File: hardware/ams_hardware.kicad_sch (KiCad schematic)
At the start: 73 parts, among them J1 USB2UART, J2 1.47 IPS LCD, J3 ConnBattery, J4 RTD_PT100, Q1 SS8050, Q2 SS8050, Q3 SS8050, SW1 RST, SW2 IN1, SW3 Boot, SW4 IN2, SW5 IN4, SW6 IN4, SW7 IN5, U1 CH340C, U2 ESP32-S3-WROOM-1, U3 TPS63001_SEPIC_3V3, U4 MAX31865xTP, U5 BQ24075RGT_DPPM

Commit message: feat: add pi zero 2 w in schematic
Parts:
- added A1: Raspberry Pi Zero v1.3, Raspberry_Pi_Zero_v.1.3_Hat:RASPI_ZERO_FULL, symbol Raspberry_Pi_Zero_v.1.3_Hat:Raspberry_Pi_Zero_v.1.3_Hat

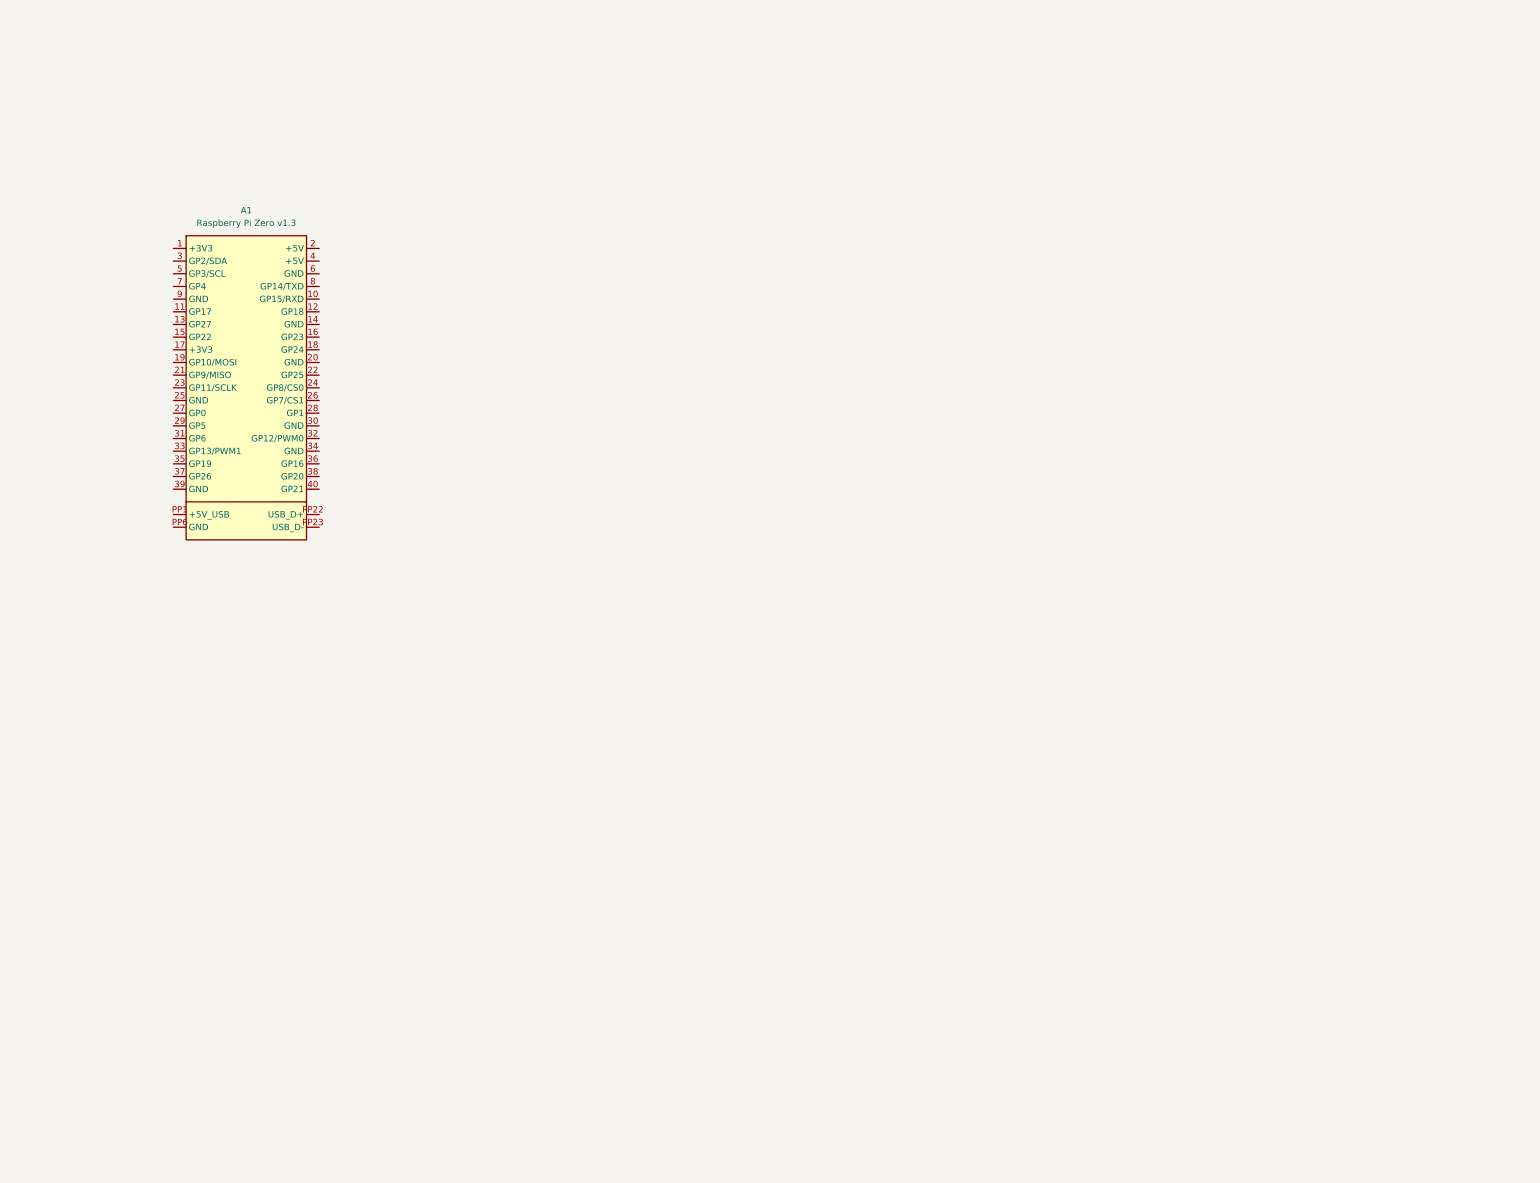
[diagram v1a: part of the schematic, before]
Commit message: feat: add logic to turn on and turn of pi
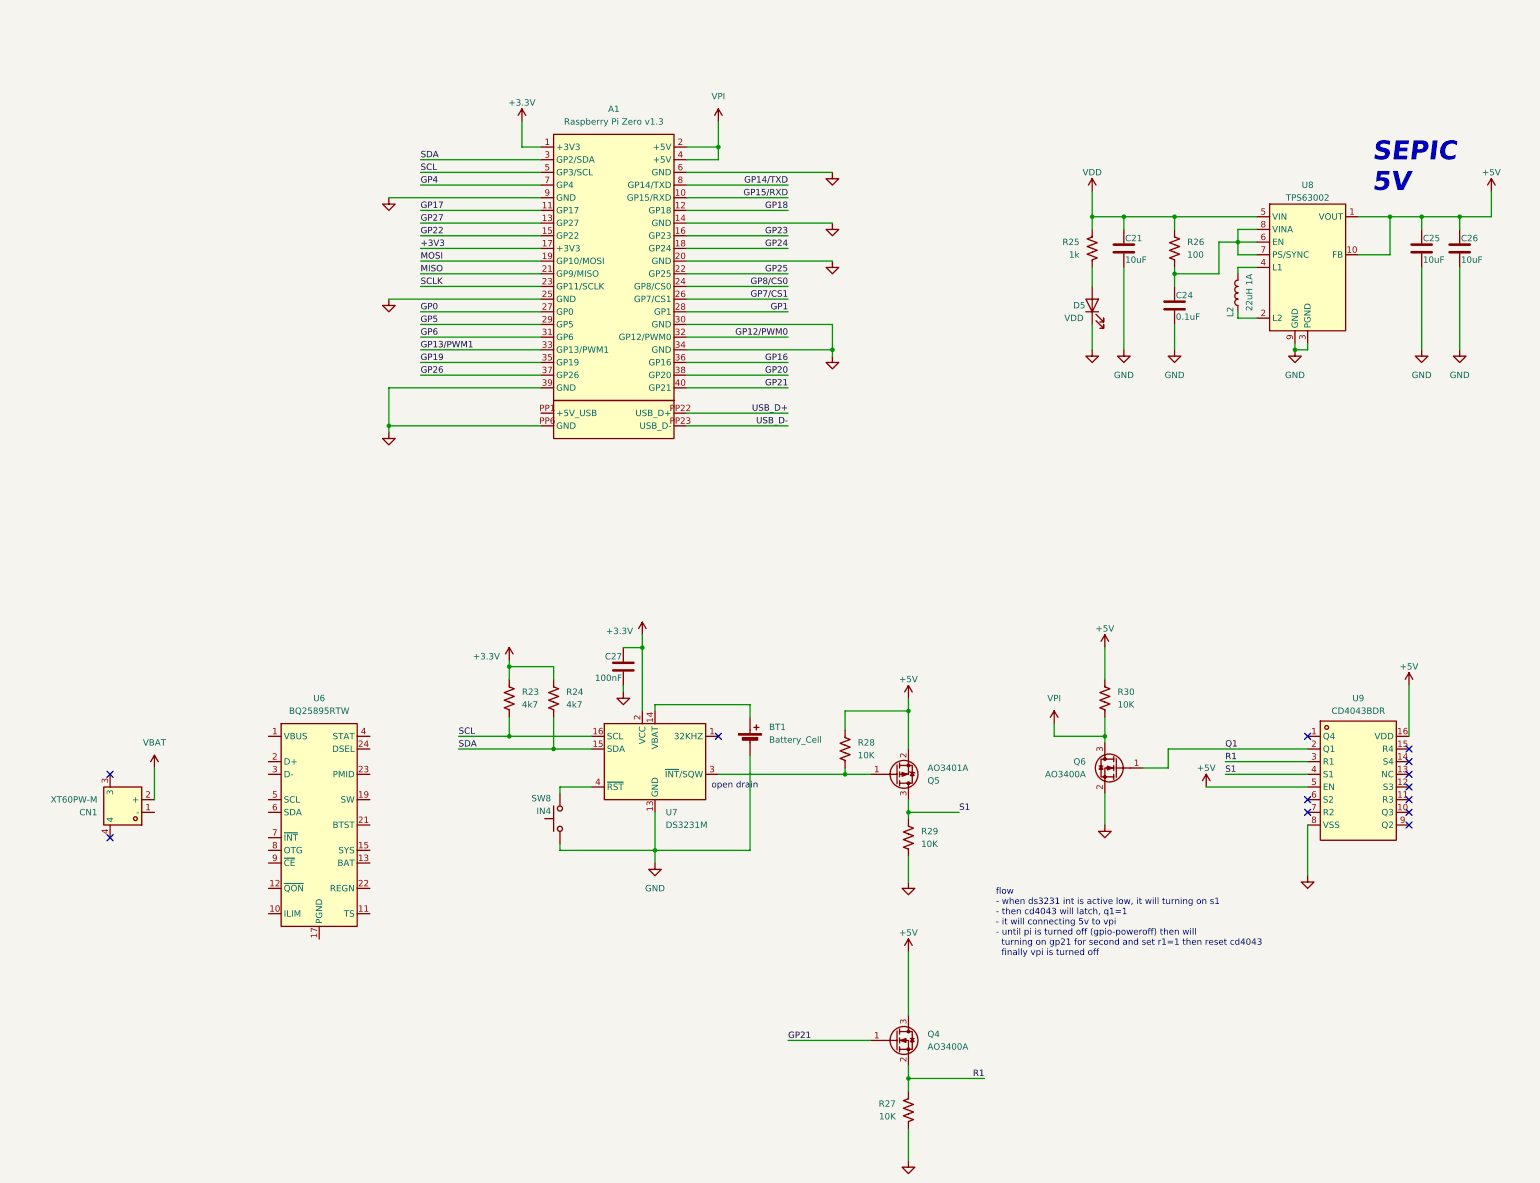
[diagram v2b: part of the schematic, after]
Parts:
- added BT1: Battery_Cell, Battery:BatteryHolder_Keystone_3002_1x2032, symbol Device:Battery_Cell
- added C21, C25, C26: 10uF, Capacitor_SMD:C_0805_2012Metric_Pad1.18x1.45mm_HandSolder, symbol Device:C
- added C24: 0.1uF, Capacitor_SMD:C_0805_2012Metric_Pad1.18x1.45mm_HandSolder, symbol Device:C
- added C27: 100nF, Capacitor_SMD:C_0805_2012Metric_Pad1.18x1.45mm_HandSolder, symbol Device:C
- added CN1: XT60PW-M, easyeda2kicad:CONN-TH_XT60PW-M, symbol easyeda2kicad:XT60PW-M
- added D5: VDD, LED_SMD:LED_1206_3216Metric_Pad1.42x1.75mm_HandSolder, symbol Device:LED
- added L2: 22uH 1A, Inductor_SMD:L_Bourns_SRP7028A_7.3x6.6mm, symbol Device:L
- added Q4, Q6: AO3400A, Package_TO_SOT_SMD:SOT-23W_Handsoldering, symbol Transistor_FET:AO3400A
- added Q5: AO3401A, Package_TO_SOT_SMD:SOT-23W_Handsoldering, symbol Transistor_FET:AO3401A
- added R23, R24: 4k7, Resistor_SMD:R_0805_2012Metric_Pad1.20x1.40mm_HandSolder, symbol Device:R_US
- added R25: 1k, Resistor_SMD:R_0805_2012Metric_Pad1.20x1.40mm_HandSolder, symbol Device:R_US
- added R26: 100, Resistor_SMD:R_0805_2012Metric_Pad1.20x1.40mm_HandSolder, symbol Device:R_US
- added R27, R28, R29, R30: 10K, Resistor_SMD:R_0805_2012Metric_Pad1.20x1.40mm_HandSolder, symbol Device:R_US
- added SW8: IN4, Button_Switch_SMD:SW_SPST_Omron_B3FS-100xP, symbol Switch:SW_Push
- added U6: BQ25895RTW, Package_DFN_QFN:Texas_RTW_WQFN-24-1EP_4x4mm_P0.5mm_EP2.7x2.7mm_ThermalVias, symbol Battery_Management:BQ25895RTW
- added U7: DS3231M, Package_SO:SOIC-16W_7.5x10.3mm_P1.27mm, symbol Timer_RTC:DS3231M
- added U8: TPS63002, Package_SON:Texas_DRC0010J_ThermalVias, symbol Regulator_Switching:TPS63002
- added U9: CD4043BDR, easyeda2kicad:SOIC-16_L9.9-W3.9-P1.27-LS6.0-BL, symbol easyeda2kicad:CD4043BDR
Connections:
- net +3.3V: now also A1.1 (+3V3), C27.1, R23.1, R24.1, U7.2 (VCC)
- net GND: now also A1.14 (GND), A1.20 (GND), A1.25 (GND), A1.30 (GND), A1.34 (GND), A1.39 (GND), A1.6 (GND), A1.9 (GND), A1.PP6 (GND), BT1.2 (-), C21.2, C24.2, C25.2, C26.2, C27.2, D5.1 (K), Q6.2 (S), R27.2, R29.2, SW8.1, U7.10 (GND), U7.11 (GND), U7.12 (GND), U7.13 (GND), U7.5 (GND), U7.6 (GND), U7.7 (GND), U7.8 (GND), U7.9 (GND), U8.11 (PGND), U8.3 (PGND), U8.9 (GND), U9.8 (VSS)
- net MISO: now also A1.21 (GP9/MISO)
- net MOSI: now also A1.19 (GP10/MOSI)
- net VDD: now also C21.1, R25.1, R26.1, U8.5 (VIN)
- net GP15/RXD: now reaches A1.10 (GP15/RXD)
- net GP17: now reaches A1.11 (GP17)
- net GP18: now reaches A1.12 (GP18)
- net GP27: now reaches A1.13 (GP27)
- net GP22: now reaches A1.15 (GP22)
- net GP23: now reaches A1.16 (GP23)
- net +3V3: now reaches A1.17 (+3V3)
- net GP24: now reaches A1.18 (GP24)
- net VPI: now reaches A1.2 (+5V)
- net VPI: now also A1.4 (+5V), Q6.3 (D), R30.2
- net GP25: now reaches A1.22 (GP25)
- net SCLK: now reaches A1.23 (GP11/SCLK)
- net GP8/CS0: now reaches A1.24 (GP8/CS0)
- net GP7/CS1: now reaches A1.26 (GP7/CS1)
- net GP0: now reaches A1.27 (GP0)
- net GP1: now reaches A1.28 (GP1)
- net GP5: now reaches A1.29 (GP5)
- net SDA: now reaches A1.3 (GP2/SDA)
- net SDA: now also R24.2, U7.15 (SDA)
- net GP6: now reaches A1.31 (GP6)
- net GP12/PWM0: now reaches A1.32 (GP12/PWM0)
- net GP13/PWM1: now reaches A1.33 (GP13/PWM1)
- net GP19: now reaches A1.35 (GP19)
- net GP16: now reaches A1.36 (GP16)
- net GP26: now reaches A1.37 (GP26)
- net GP20: now reaches A1.38 (GP20)
- net GP21: now reaches A1.40 (GP21)
- net GP21: now also Q4.1 (G)
- net SCL: now reaches A1.5 (GP3/SCL)
- net SCL: now also R23.2, U7.16 (SCL)
- net GP4: now reaches A1.7 (GP4)
- net GP14/TXD: now reaches A1.8 (GP14/TXD)
- net USB_D+: now reaches A1.PP22 (USB_D+)
- net USB_D-: now reaches A1.PP23 (USB_D-)
- new net: Q5.1 (G), R28.2, U7.3 (~{INT}/SQW)
- new net: D5.2 (A), R25.2
- new net: BT1.1 (+), U7.14 (VBAT)
- new net: SW8.2, U7.4 (~{RST})
- new net: C24.1, R26.2, U8.6 (EN), U8.7 (PS/SYNC), U8.8 (VINA)
- new net: U6.13 (BAT), U6.14 (BAT)
- new net: U6.15 (SYS), U6.16 (SYS)
- new net: U6.17 (PGND), U6.18 (PGND), U6.25 (PGND)
- new net: U6.19 (SW), U6.20 (SW)
- new net: L2.1, U8.2 (L2)
- new net: L2.2, U8.4 (L1)
- new net +5V: C25.1, C26.1, Q4.3 (D), Q5.2 (S), R28.1, R30.1, U8.1 (VOUT), U8.10 (FB), U9.16 (VDD), U9.5 (EN)
- new net Q1: Q6.1 (G), U9.2 (Q1)
- new net R1: Q4.2 (S), R27.1, U9.3 (R1)
- new net S1: Q5.3 (D), R29.1, U9.4 (S1)
- new net VBAT: CN1.2 (+)
- no-connect marks 24 -> 37
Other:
- note added: "SEPIC 5V"
- note added: "flow - when ds3231 int is active low, it will turning on s1 - then cd4043 will latch, q1=1 - it will connecting 5v to vpi - until pi is turned off (gpio-poweroff) then will turning on gp21 for second and set r1=1 then reset cd4043 finally vpi is turned off"
- note added: "open drain"
- moved on the sheet: A1
